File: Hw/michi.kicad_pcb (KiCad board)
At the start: 2 copper layers, 63 parts, among them J1 Conn_01x02, J2 Conn_Right, P1 USB_C_Plug_USB2.0, P6 D, SW1 SW_Push, U1 RP2040, U2 NCP1117ST33T3G, U3 W25Q128JVS, Y1 Crystal

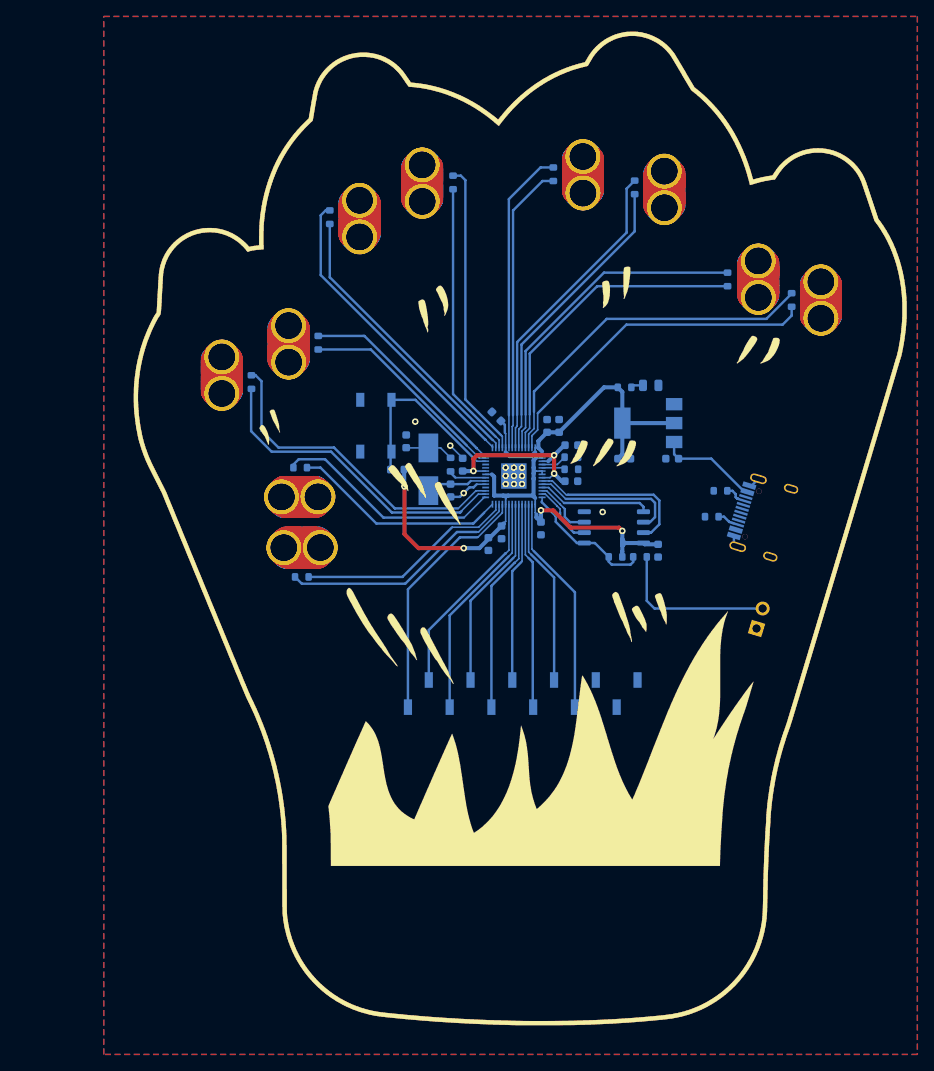
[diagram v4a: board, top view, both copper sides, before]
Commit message: Resisitive sensors connected
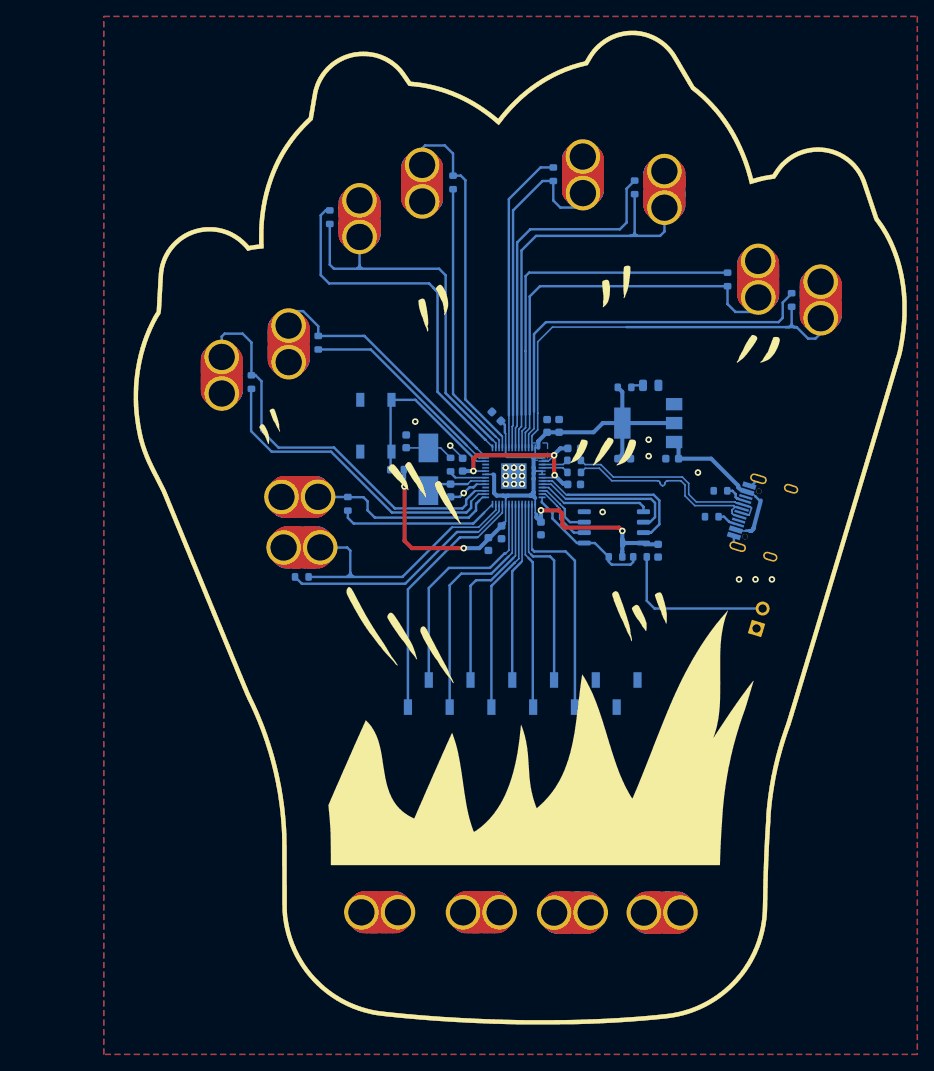
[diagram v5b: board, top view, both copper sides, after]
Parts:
- removed the P6 at (90.4, 94.9)
- removed the P6 at (134.9, 57.4)
- removed the P6 at (90.7, 101.1)
- removed the P6 at (125.1, 55.6)
- removed the P6 at (146.4, 68.3)
- removed the P6 at (81.1, 80.0)
- removed the P6 at (105.5, 56.6)
- removed the P6 at (154.0, 70.9)
- removed the P6 at (89.2, 76.2)
- removed the P6 at (97.9, 61.0)
- added P6: D, SEWALLI_renew, F.Cu at (112.5, 145.5)
- added P6: D, SEWALLI_renew, F.Cu at (134.5, 145.5)
- added P6: D, SEWALLI_renew, F.Cu at (100.1, 145.5)
- added P6: D, SEWALLI_renew, F.Cu at (123.6, 145.5)
- moved R7 7.28 mm to (96.4, 95.8), turned to -90 degrees
- moved C10 0.52 mm to (123.9, 93.4)
- moved C12 0.52 mm to (123.9, 89.1)
- moved R3 0.51 mm to (123.9, 90.5)
- moved R4 0.51 mm to (123.9, 92.0)
- moved Ref** 0.10 mm to (117.4, 98.7)
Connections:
- J2 pad 10: unconnected-(J2-Pad10) -> GND
- J2 pad 11: unconnected-(J2-Pad11) -> GND
- J2 pad 12: unconnected-(J2-Pad12) -> GND
- P6 pad 1: (no net) -> /IO25
- P6 pad 1: (no net) -> /IO21
- P6 pad 1: (no net) -> /IO27
- P6 pad 1: (no net) -> /IO23
- P6 pad 1: (no net) -> /IO29
- P6 pad 1: (no net) -> /IO12
- P6 pad 1: (no net) -> /IO10
- P6 pad 1: (no net) -> /IO14
- P6 pad 1: (no net) -> /IO17
- P6 pad 1: (no net) -> /IO19
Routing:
- net /D-: track 0.00 -> 24.2 mm
- net /D+: track 0.00 -> 24.0 mm
- net /IO25: track 36.7 -> 51.3 mm
- net /IO29: track 41.4 -> 54.7 mm
- net /IO19: track 35.6 -> 47.9 mm
- net /IO27: track 39.1 -> 50.8 mm
- net /IO14: track 39.6 -> 50.6 mm
- net /IO21: track 36.2 -> 45.2 mm
- net VBUS: track 12.3 -> 20.8 mm
- net /IO10: track 26.9 -> 35.1 mm
- net /IO18: track 38.3 -> 46.2 mm
- net /IO23: track 35.3 -> 42.9 mm
- net /IO17: track 26.3 -> 33.2 mm
- net /IO11: track 26.4 -> 19.7 mm
- net /IO24: track 38.5 -> 44.9 mm
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- added copper zone on B.Cu, net +3V3

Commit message: Edge.Cuts generated
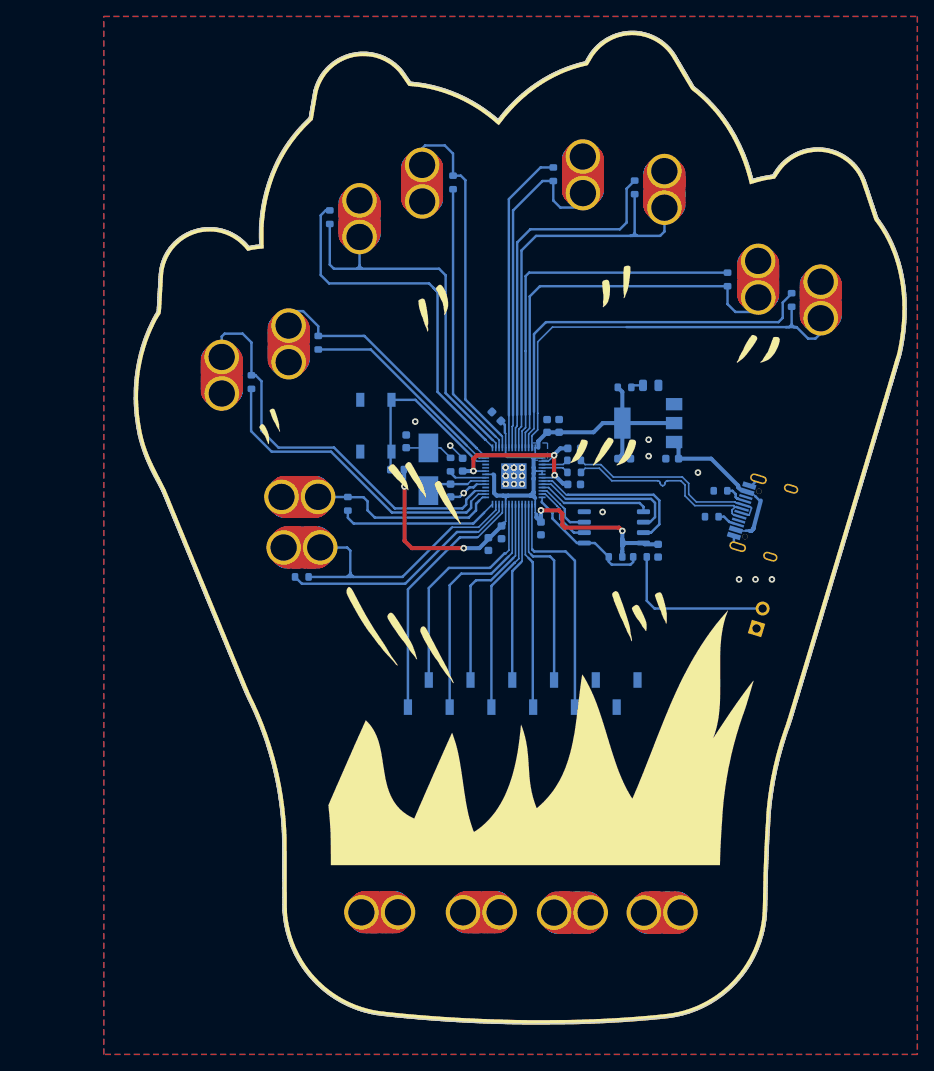
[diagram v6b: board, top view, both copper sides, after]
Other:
- board outline added: 93.9 x 120.8 mm
